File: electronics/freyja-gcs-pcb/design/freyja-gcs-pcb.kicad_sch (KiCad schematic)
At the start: 32 parts, among them J1 Conn_01x07_Pin, SW1 SW_SPST, SW2 SW_SPST, U1 STM32U575RGTx, U2 GT-USB-7010ASV, U9 SN65HVD232DR, Y1 48MHz, Y2 32768Hz

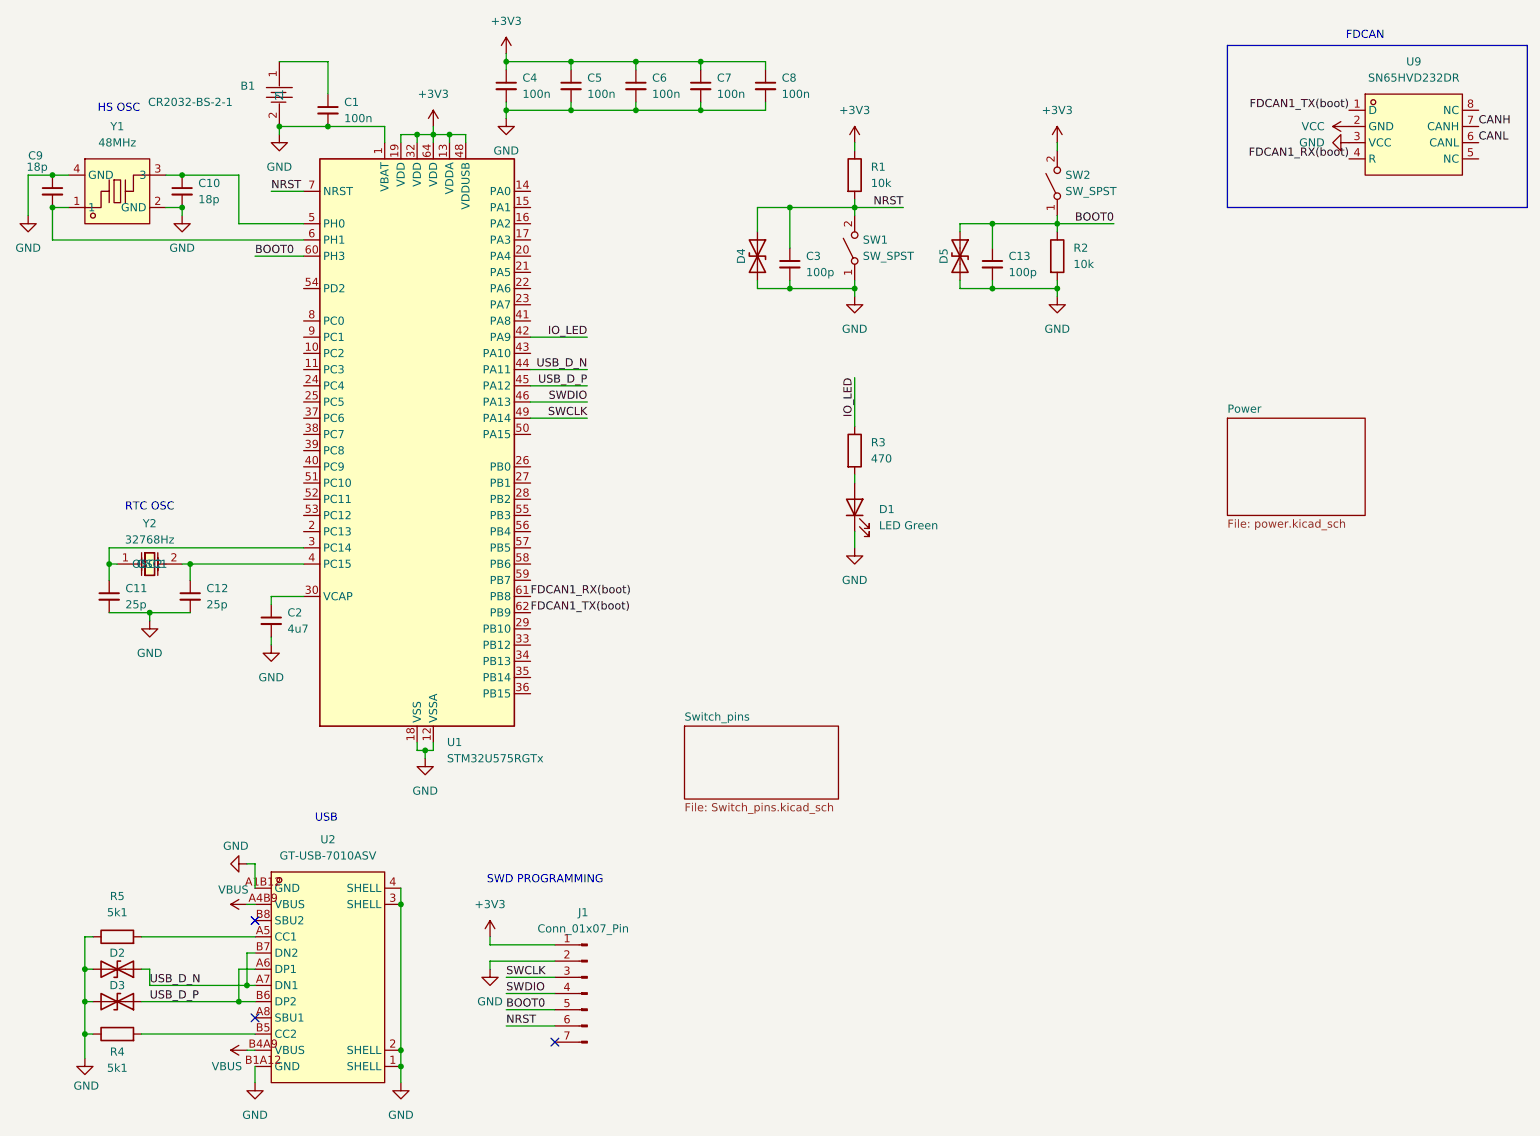
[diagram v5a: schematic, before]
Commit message: reset annotation
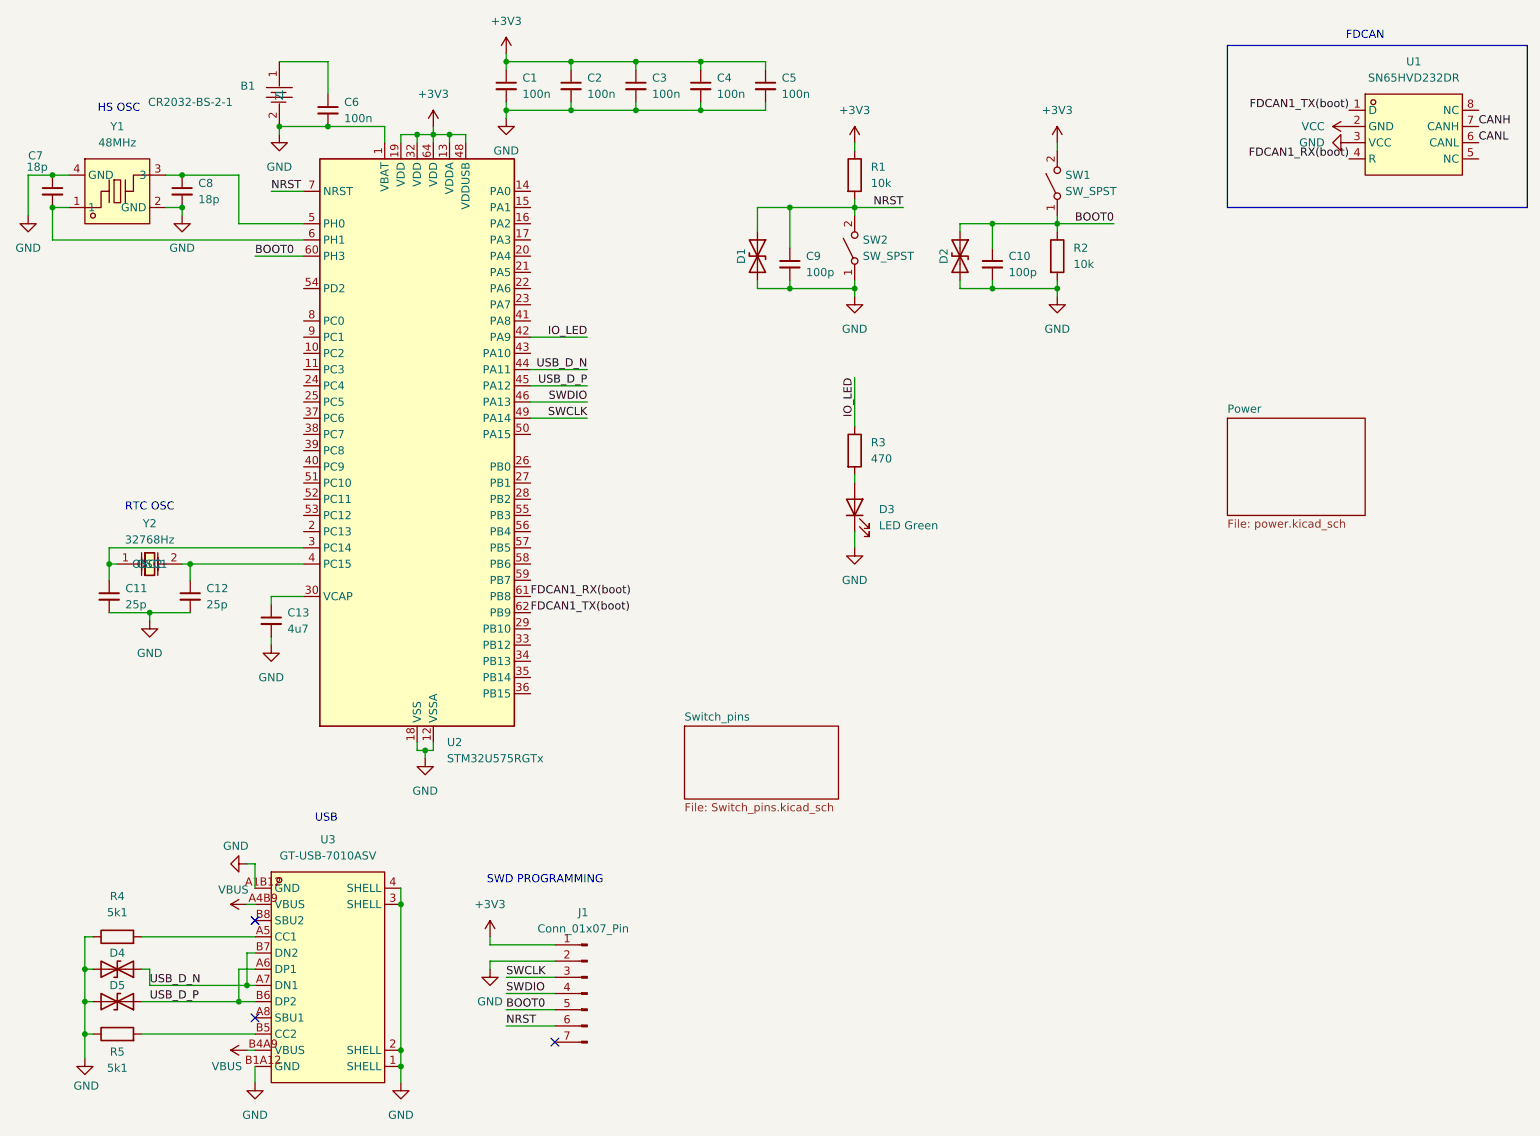
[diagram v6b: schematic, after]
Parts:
- renumbered C4 to C1, C13 to C10, C2 to C13, C5 to C2, C6 to C3, C7 to C4, C8 to C5, C1 to C6, C9 to C7, C10 to C8, C3 to C9, D4 to D1, D5 to D2, D1 to D3, D2 to D4, D3 to D5, R5 to R4, R4 to R5, SW2 to SW1, SW1 to SW2, U9 to U1, U1 to U2, U2 to U3

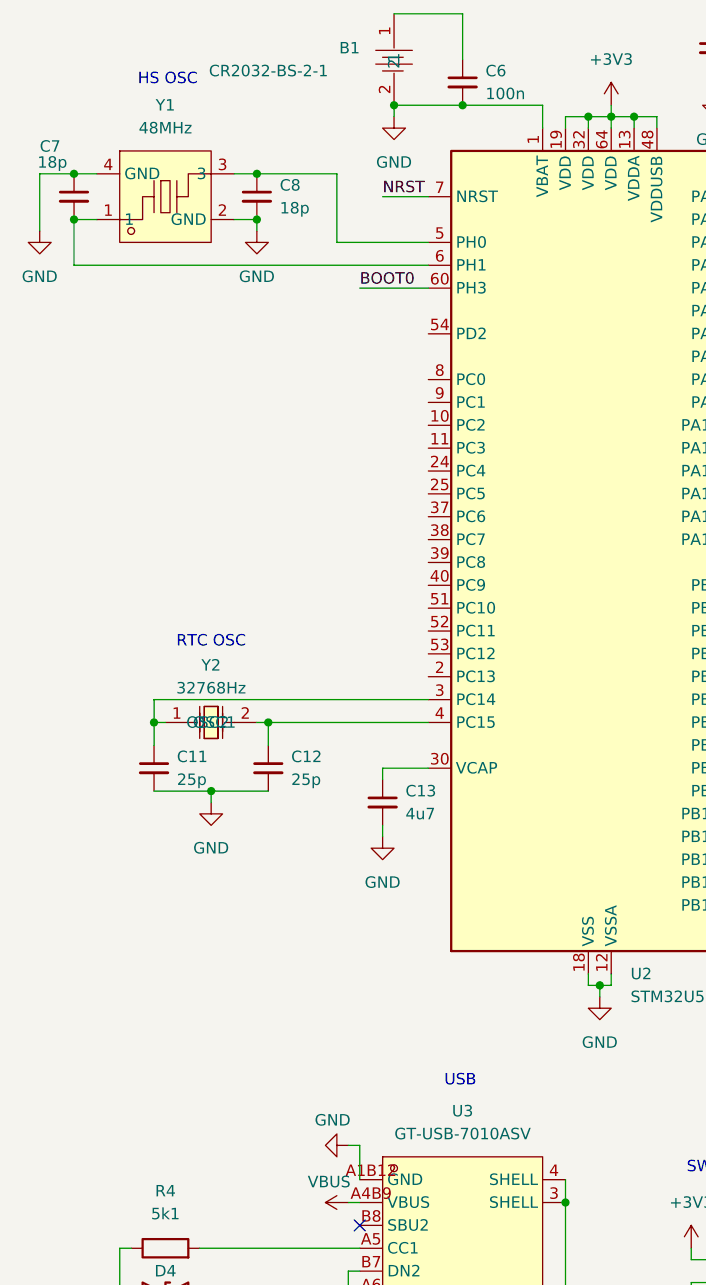
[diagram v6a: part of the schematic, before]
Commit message: add led backlight driver
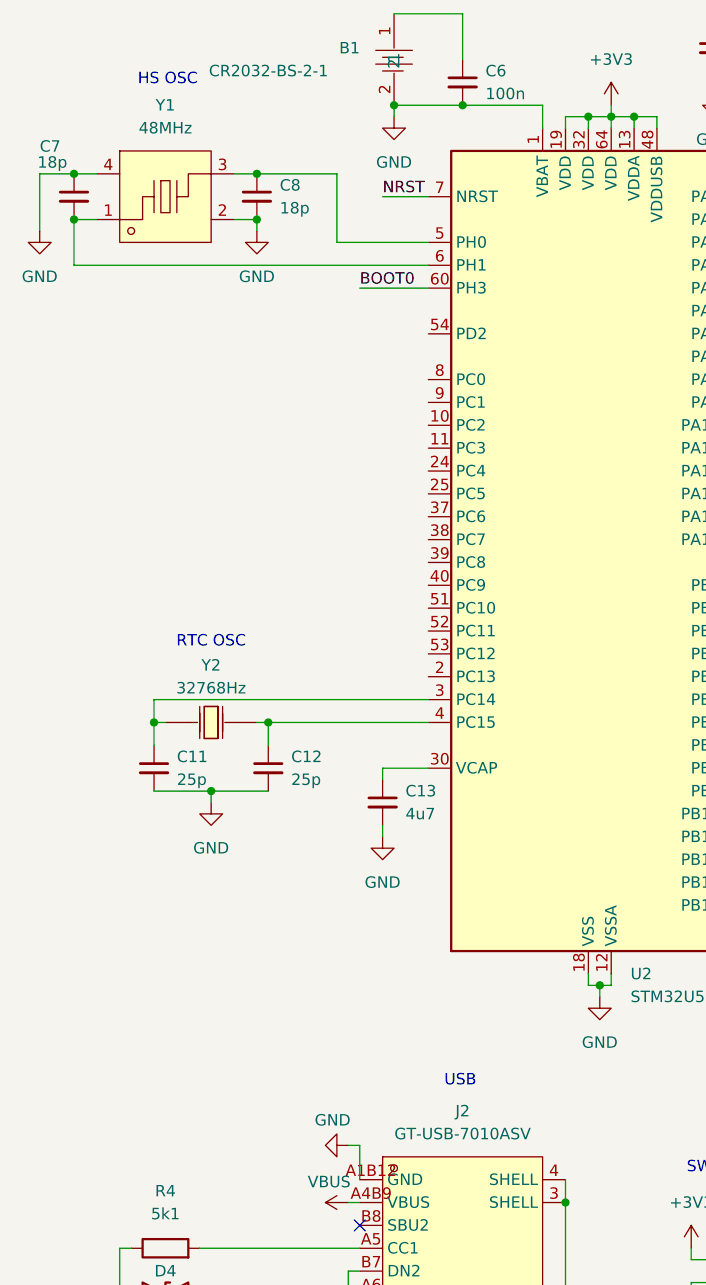
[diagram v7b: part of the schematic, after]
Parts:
- renumbered U3 to J2
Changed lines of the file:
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@@
 		(dnp no)
 		(fields_autoplaced yes)
-		(property "Reference" "U3"
+		(property "Reference" "J2"
 			(at 64.77 142.24 0)
 			(effects
@@
 			(project ""
 				(path "/c292fa04-82ad-49e9-a9d8-422554d1d11d"
-					(reference "U3")
+					(reference "J2")
 					(unit 1)
 				)

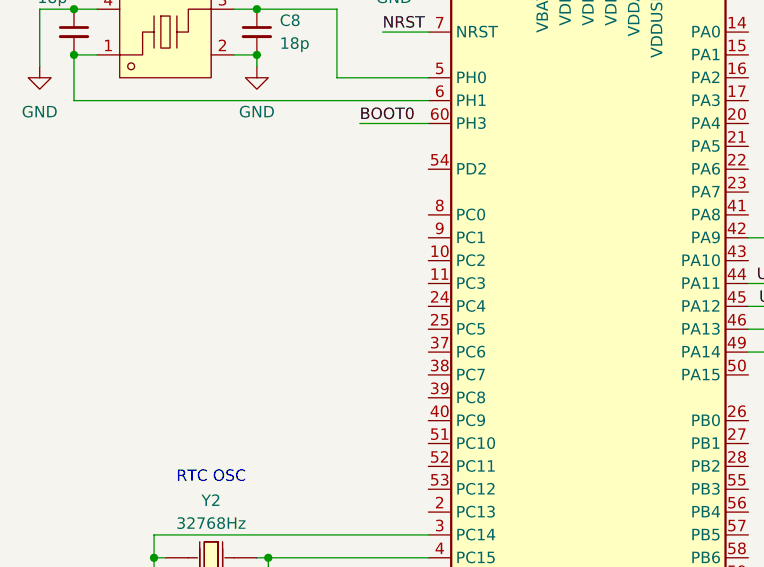
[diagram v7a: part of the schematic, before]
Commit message: fan connector
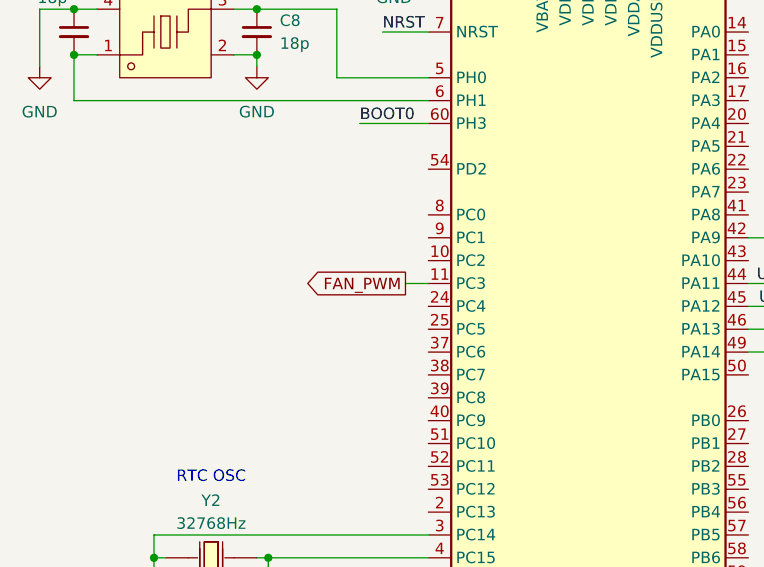
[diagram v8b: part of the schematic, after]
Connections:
- net FAN_PWM: now reaches U2.11 (PC3)
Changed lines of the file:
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@@
+	(wire
+		(pts
+			(xy 58.42 68.58) (xy 60.96 68.58)
+		)
+		(stroke
+			(width 0)
+			(type default)
+		)
+	)
 	(wire
 		(pts
@@
 		)
 	)
+	(global_label "FAN_PWM"
+		(shape output)
+		(at 58.42 68.58 180)
+		(fields_autoplaced yes)
+		(effects
+			(font
+				(size 1.27 1.27)
+			)
+			(justify right)
+		)
+		(property "Intersheetrefs" "${INTERSHEET_REFS}"
+			(at 46.7867 68.58 0)
+			(effects
+				(font
+					(size 1.27 1.27)
+				)
+				(justify right)
+				(hide yes)
+			)
+		)
+	)
